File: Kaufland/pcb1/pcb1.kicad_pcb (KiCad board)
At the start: 2 copper layers, 118.4 x 66.5 mm, 15 parts, among them J1 AudioJack2, J2 Barrel_Jack, SW1 SW_Push, U1 DF_Player, U2 RGB_LED_STRIP

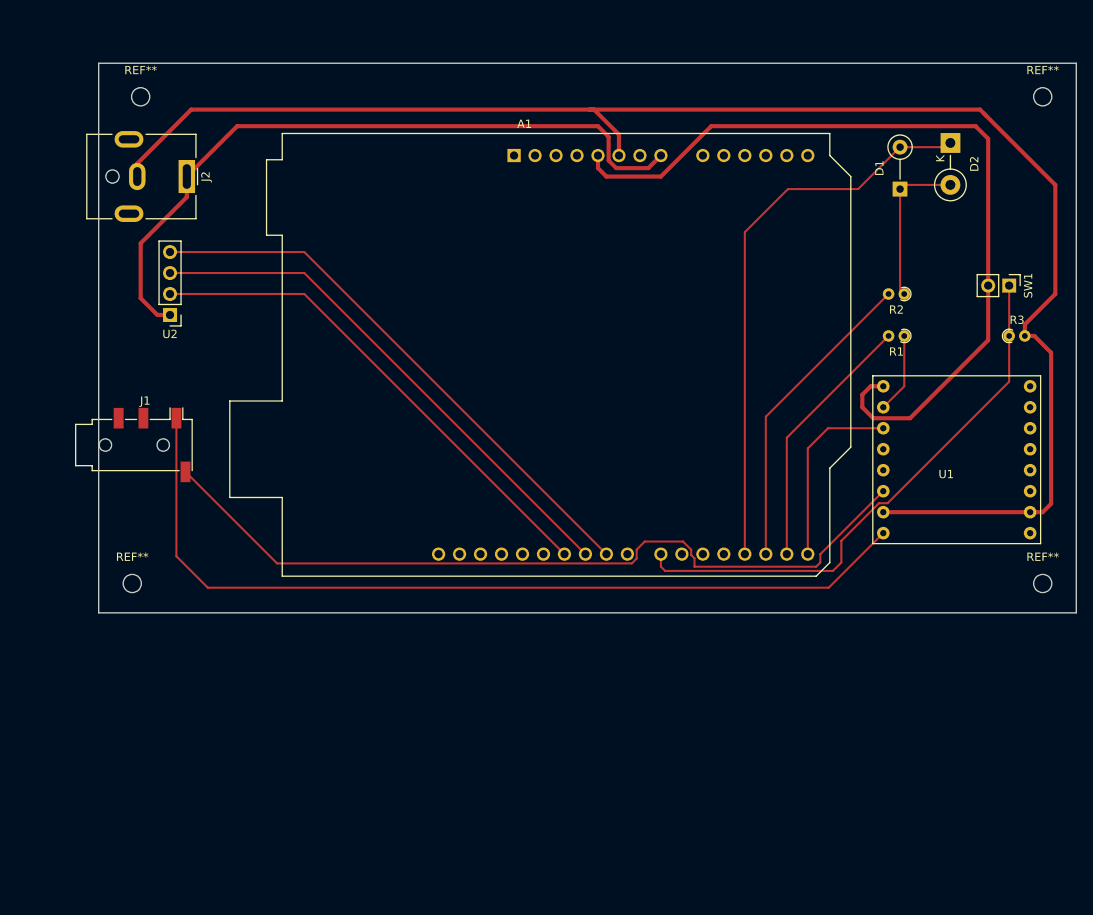
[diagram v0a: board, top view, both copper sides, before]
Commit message: Flipped pcb (to be checked; routed)
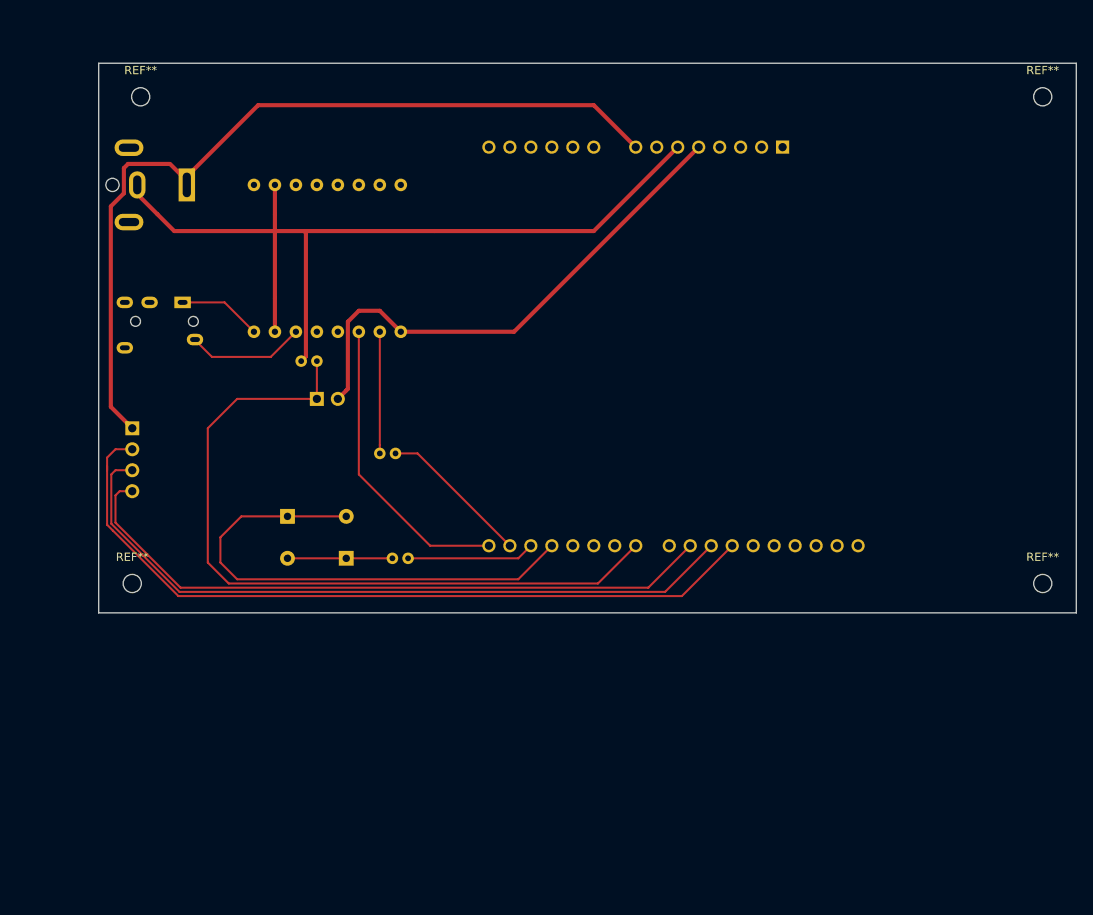
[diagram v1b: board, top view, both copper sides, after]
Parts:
- A1, D1, J2, R1, R2, R3, SW1, U1, U2: moved to B.Cu
- D2: footprint Diode_THT:D_DO-15_P5.08mm_Vertical_KathodeUp -> Diode_THT:D_A-405_P5.08mm_Vertical_KathodeUp; moved to B.Cu
- J1: footprint Connector_Audio:Jack_3.5mm_PJ320D_Horizontal -> Connector_Audio:Jack_3.5mm_PJ320E_Horizontal; moved to B.Cu
- moved D2 92.1 mm to (72.6, 105.2)
- moved SW1 84.9 mm to (76.2, 90.9)
- moved R3 83.9 mm to (76.2, 86.4), turned to 180 degrees
- moved D1 80.6 mm to (79.8, 110.2)
- moved U1 80.0 mm to (76.2, 75.2), turned to 90 degrees
- moved R2 69.8 mm to (85.3, 110.2), turned to 0 degrees
- moved R1 65.1 mm to (83.8, 97.5), turned to 0 degrees
- moved A1 32.5 mm to (132.6, 60.5), turned to 180 degrees
- moved J1 17.9 mm to (59.9, 79.2), turned to 270 degrees
- moved U2 14.5 mm to (53.8, 94.5)
- moved J2 1.02 mm to (60.5, 65.0), turned to 90 degrees
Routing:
- net Net-(J1-PadT): track 106.6 -> 10.1 mm
- net GNDREF: track 189.8 -> 105.4 mm
- net Net-(J1-PadS): track 97.4 -> 14.4 mm
- net +5V: track 104.6 -> 63.2 mm
- net Net-(A1-Pad26): track 60.8 -> 93.9 mm
- net Net-(A1-Pad22): track 66.6 -> 90.3 mm
- net Net-(A1-Pad25): track 64.4 -> 87.1 mm
- net Net-(A1-Pad17): track 37.7 -> 15.5 mm
- net +12V: track 85.8 -> 103.0 mm
- net Net-(A1-Pad15): track 22.9 -> 36.6 mm
- net Net-(A1-Pad16): track 31.5 -> 18.5 mm
- net Net-(A1-Pad24): track 68.0 -> 80.5 mm
- net Net-(D1-Pad1): track 19.2 -> 12.7 mm
- net Net-(A1-Pad18): track 68.3 -> 62.0 mm
- net Net-(R1-Pad1): track 9.69 -> 14.7 mm

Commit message: small changes to the pcb
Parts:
- R1, R2, R3: footprint Resistor_THT:R_Axial_DIN0204_L3.6mm_D1.6mm_P1.90mm_Vertical -> Resistor_THT:R_Axial_DIN0204_L3.6mm_D1.6mm_P7.62mm_Horizontal
- moved R3 14.8 mm to (68.6, 99.1), turned to 90 degrees
- moved R1 6.37 mm to (86.9, 91.9), turned to 270 degrees
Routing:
- net GNDREF: track 105.4 -> 118.4 mm
- net Net-(A1-Pad22): track 90.3 -> 79.2 mm
- net Net-(A1-Pad16): track 18.5 -> 28.0 mm
- net Net-(A1-Pad17): track 15.5 -> 9.78 mm
- net Net-(R1-Pad1): track 14.7 -> 10.4 mm

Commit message: finished pcb v1.0
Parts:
- removed A1: Arduino_UNO_R3, Module:Arduino_UNO_R3
- removed J1: AudioJack2, Connector_Audio:Jack_3.5mm_PJ320E_Horizontal
- removed J2: Barrel_Jack, Connector_BarrelJack:BarrelJack_CUI_PJ-063AH_Horizontal
- removed R1: 1k, Resistor_THT:R_Axial_DIN0204_L3.6mm_D1.6mm_P7.62mm_Horizontal
- removed R2: 330, Resistor_THT:R_Axial_DIN0204_L3.6mm_D1.6mm_P7.62mm_Horizontal
- removed the REF** at (164.1, 54.4)
- removed the REF** at (164.1, 113.3)
- removed the REF** at (53.8, 113.3)
- removed the REF** at (54.9, 54.4)
- removed U1: DF_Player, pcb1:DFPlayerMini
- removed U2: RGB_LED_STRIP, Connector_PinHeader_2.54mm:PinHeader_1x04_P2.54mm_Vertical
- added Arduino: Arduino_UNO_R3, Module:Arduino_UNO_R3, F.Cu at (112.8, 63.5)
- added Audio jack: AudioJack2, Connector_Audio:Jack_3.5mm_PJ320E_Horizontal, F.Cu at (55.9, 77.7)
- added Barrel Jack: Barrel_Jack, Connector_BarrelJack:BarrelJack_CUI_PJ-063AH_Horizontal, F.Cu at (57.9, 99.6)
- added D3: LED, Connector:FanPinHeader_1x03_P2.54mm_Vertical, F.Cu at (124.5, 121.9)
- added D4: LED, Connector:FanPinHeader_1x03_P2.54mm_Vertical, F.Cu at (127.0, 131.6)
- added DF Player: DF_Player, pcb1:DFPlayerMini, F.Cu at (66.5, 58.4)
- added Q1: IRLB8721PBF, Package_TO_SOT_THT:TO-220-3_Vertical, F.Cu at (50.8, 124.5)
- added Q2: IRLB8721PBF, Package_TO_SOT_THT:TO-220-3_Vertical, F.Cu at (53.3, 132.6)
- added Q3: IRLB8721PBF, Package_TO_SOT_THT:TO-220-3_Vertical, F.Cu at (55.9, 140.7)
- added Q4: IRLB8721PBF, Package_TO_SOT_THT:TO-220-3_Vertical, F.Cu at (91.9, 134.1)
- added Q5: IRLB8721PBF, Package_TO_SOT_THT:TO-220-3_Vertical, F.Cu at (100.1, 131.6)
- added Q6: IRLB8721PBF, Package_TO_SOT_THT:TO-220-3_Vertical, F.Cu at (108.2, 129.0)
- added R1 1k: 1k, Resistor_THT:R_Axial_DIN0204_L3.6mm_D1.6mm_P7.62mm_Horizontal, F.Cu at (67.6, 83.8)
- added R2 330: 330, Resistor_THT:R_Axial_DIN0204_L3.6mm_D1.6mm_P7.62mm_Horizontal, F.Cu at (144.8, 128.0)
- added R4 330: 330, Resistor_THT:R_Axial_DIN0204_L3.6mm_D1.6mm_P7.62mm_Horizontal, F.Cu at (130.6, 127.5)
- added R5: 4.7k, Resistor_THT:R_Axial_DIN0204_L3.6mm_D1.6mm_P7.62mm_Horizontal, F.Cu at (117.0, 49.8)
- added REF**: MountingHole_2.2mm_M2, MountingHole:MountingHole_2.2mm_M2, F.Cu at (50.8, 48.3)
- added REF**: MountingHole_2.2mm_M2, MountingHole:MountingHole_2.2mm_M2, F.Cu at (153.4, 48.3)
- added REF**: MountingHole_2.2mm_M2, MountingHole:MountingHole_2.2mm_M2, F.Cu at (153.4, 147.8)
- added REF**: MountingHole_2.2mm_M2, MountingHole:MountingHole_2.2mm_M2, F.Cu at (50.8, 147.8)
- added RGB LED Strip 1: RGB_LED_STRIP-My_Library, Connector:FanPinHeader_1x04_P2.54mm_Vertical, F.Cu at (53.3, 114.3)
- added RGB LED Strip 2: RGB_LED_STRIP-My_Library, Connector:FanPinHeader_1x04_P2.54mm_Vertical, F.Cu at (81.8, 131.6)
- added SW2: SW_Push, Connector:FanPinHeader_1x03_P2.54mm_Vertical, F.Cu at (122.9, 50.8)
- D1, D2: footprint Diode_THT:D_A-405_P5.08mm_Vertical_KathodeUp -> Connector:FanPinHeader_1x03_P2.54mm_Vertical; moved to F.Cu
- R3: moved to F.Cu
- SW1: footprint Connector_PinHeader_2.54mm:PinHeader_1x02_P2.54mm_Vertical -> Connector:FanPinHeader_1x03_P2.54mm_Vertical; moved to F.Cu
- moved D2 68.3 mm to (138.7, 122.4), turned to 0 degrees
- moved R3 66.9 mm to (113.9, 49.8), turned to 270 degrees
- moved D1 65.2 mm to (141.2, 132.0), turned to 180 degrees
- moved SW1 51.3 mm to (108.2, 50.8)
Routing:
- net GNDREF: track 118.4 -> 231.7 mm
- net Net-(A1-Pad18): track 0.00 -> 112.0 mm, vias 0 -> 3
- net Net-(A1-Pad20): track 0.00 -> 104.1 mm, vias 0 -> 3
- net Net-(A1-Pad21): track 0.00 -> 95.7 mm, vias 0 -> 3
- net Net-(A1-Pad28): track 0.00 -> 80.6 mm, vias 0 -> 2
- net Net-(A1-Pad15): track 36.6 -> 105.8 mm, vias 0 -> 1
- net Net-(A1-Pad25): track 87.1 -> 30.4 mm
- net Net-(A1-Pad24): track 80.5 -> 23.8 mm
- net Net-(A1-Pad26): track 93.9 -> 37.7 mm
- net Net-(A1-Pad16): track 28.0 -> 82.2 mm
- net Net-(A1-Pad19): track 62.0 -> 21.2 mm
- net +12V: track 103.0 -> 140.4 mm
- net Net-(Q3-Pad3): track 0.00 -> 26.4 mm
- net Net-(Q6-Pad3): track 0.00 -> 26.4 mm
- net Net-(A1-Pad22): track 0.00 -> 24.2 mm
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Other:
- board size 118.4 x 66.5 mm -> 109.7 x 106.7 mm
- board text added: "4,7k"
- board text added: "Audio sistem version: 1.0"

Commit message: Changed pins for LED strips
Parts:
- J1: renamed from Audio jack
- J2: renamed from Barrel Jack
- R1: renamed from R1 1k
- R2: renamed from R2 330
- R4: renamed from R4 330
- U1: renamed from DF Player
- U2: renamed from RGB LED Strip 1; footprint Connector:FanPinHeader_1x04_P2.54mm_Vertical -> Connector_JST:JST_EH_S4B-EH_1x04_P2.50mm_Horizontal
- U3: renamed from RGB LED Strip 2; footprint Connector:FanPinHeader_1x04_P2.54mm_Vertical -> Connector_JST:JST_EH_S4B-EH_1x04_P2.50mm_Horizontal
- moved U3 29.7 mm to (52.8, 138.2)
- moved Q2 26.2 mm to (79.2, 136.1)
- moved Q1 26.2 mm to (76.7, 128.0)
- moved Q3 26.2 mm to (81.8, 144.3)
- moved U2 7.13 mm to (52.8, 121.4), turned to 90 degrees
- moved Q4 0.51 mm to (91.9, 134.6)
- renumbered Arduino to A1
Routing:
- net Net-(Q3-Pad3): track 26.4 -> 68.1 mm
- net Net-(Q2-Pad3): track 18.3 -> 54.9 mm, vias 0 -> 1
- net Net-(Q5-Pad3): track 18.3 -> 51.3 mm, vias 0 -> 1
- net Net-(Q6-Pad3): track 26.4 -> 58.2 mm, vias 0 -> 1
- net Net-(Q4-Pad3): track 10.2 -> 41.7 mm
- net +12V: track 140.4 -> 112.1 mm
- net Net-(Q1-Pad3): track 10.2 -> 37.2 mm, vias 0 -> 4
- net GNDREF: track 231.7 -> 235.3 mm, vias 0 -> 1
- net Net-(A1-Pad21): track 95.7 -> 94.0 mm
- net Net-(A1-Pad20): track 104.1 -> 102.6 mm
- net Net-(A1-Pad18): track 112.0 -> 113.1 mm, vias 3 -> 2

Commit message: bugfixing pcb
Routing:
- net +12V: track 112.1 -> 131.1 mm
- net GNDREF: track 235.3 -> 234.2 mm, vias 1 -> 3
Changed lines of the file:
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@@
-(kicad_pcb (version 20171130) (host pcbnew "(5.1.6)-1")
+(kicad_pcb (version 20171130) (host pcbnew "(5.1.5)-3")
   (general
     (thickness 1.6)
     (drawings 12)
-    (tracks 236)
+    (tracks 246)
     (zones 0)
     (modules 27)
@@
   )
   (setup
-    (last_trace_width 0.25)
+    (last_trace_width 0.5)
     (user_trace_width 0.5)
     (trace_clearance 0.2)
@@
   (segment (start 108.712 120.396) (end 110.236 120.396) (width 0.25) (layer B.Cu) (net 11))
   (segment (start 118.876 111.76) (end 110.236 120.396) (width 0.25) (layer B.Cu) (net 11))
-  (segment (start 106.87899 123.422839) (end 107.873829 122.428) (width 0.25) (layer B.Cu) (net 13))
-  (segment (start 106.87899 124.81651) (end 106.87899 123.422839) (width 0.25) (layer B.Cu) (net 13))
+  (segment (start 110.744 122.428) (end 121.416 111.76) (width 0.25) (layer B.Cu) (net 13))
   (segment (start 100.076 131.572) (end 100.1235 131.572) (width 0.25) (layer B.Cu) (net 13))
+  (segment (start 106.87899 124.81651) (end 106.87899 123.24501) (width 0.25) (layer B.Cu) (net 13))
   (segment (start 100.1235 131.572) (end 106.87899 124.81651) (width 0.25) (layer B.Cu) (net 13))
-  (segment (start 110.748 122.428) (end 121.416 111.76) (width 0.25) (layer B.Cu) (net 13))
-  (segment (start 107.873829 122.428) (end 110.748 122.428) (width 0.25) (layer B.Cu) (net 13))
+  (segment (start 106.87899 123.24501) (end 107.696 122.428) (width 0.25) (layer B.Cu) (net 13))
+  (segment (start 107.696 122.428) (end 110.744 122.428) (width 0.25) (layer B.Cu) (net 13))
   (segment (start 123.956 111.76) (end 112.272 123.444) (width 0.25) (layer B.Cu) (net 15))
   (segment (start 112.272 123.444) (end 112.268 123.444) (width 0.25) (layer B.Cu) (net 15))
@@
   (segment (start 57.912 116.332) (end 52.832 121.412) (width 0.5) (layer B.Cu) (net 16))
   (segment (start 57.912 109.22) (end 57.912 116.332) (width 0.5) (layer B.Cu) (net 16))
+  (segment (start 51.857 121.412) (end 50.8 122.469) (width 0.5) (layer B.Cu) (net 16))
+  (segment (start 52.832 121.412) (end 51.857 121.412) (width 0.5) (layer B.Cu) (net 16))
+  (segment (start 50.8 122.469) (end 50.8 136.144) (width 0.5) (layer B.Cu) (net 16))
+  (segment (start 50.8 136.144) (end 52.832 138.176) (width 0.5) (layer B.Cu) (net 16))
   (segment (start 124.46 123.185) (end 124.46 131.572) (width 0.25) (layer F.Cu) (net 17))
   (segment (start 124.46 121.92) (end 124.46 123.185) (width 0.25) (layer F.Cu) (net 17))
@@
   (segment (start 131.581001 134.102999) (end 131.255999 134.428001) (width 0.25) (layer F.Cu) (net 19))
   (segment (start 130.556 111.76) (end 131.581001 112.785001) (width 0.25) (layer F.Cu) (net 19))
-  (segment (start 71.628 48.26) (end 71.628 66.04) (width 0.5) (layer B.Cu) (net 20))
   (segment (start 80.772 57.404) (end 82.804 57.404) (width 0.5) (layer B.Cu) (net 20))
   (segment (start 71.628 48.26) (end 80.772 57.404) (width 0.5) (layer B.Cu) (net 20))
-  (segment (start 113.88 57.448) (end 82.804 57.404) (width 0.5) (layer B.Cu) (net 20))
   (segment (start 82.804 57.404) (end 80.816 57.448) (width 0.5) (layer B.Cu) (net 20))
   (segment (start 113.88 57.448) (end 117.03 57.448) (width 0.5) (layer B.Cu) (net 20))
@@
   (segment (start 117.03 57.448) (end 119.424 57.448) (width 0.5) (layer B.Cu) (net 20))
   (segment (start 119.424 57.448) (end 124.676001 62.700001) (width 0.5) (layer B.Cu) (net 20))
-  (segment (start 75.380001 73.949999) (end 51.912 97.418) (width 0.5) (layer F.Cu) (net 20))
-  (segment (start 75.380001 65.458239) (end 75.380001 73.949999) (width 0.5) (layer F.Cu) (net 20))
   (segment (start 51.912 97.418) (end 51.912 99.568) (width 0.5) (layer F.Cu) (net 20))
-  (segment (start 74.749761 64.827999) (end 75.380001 65.458239) (width 0.5) (layer F.Cu) (net 20))
-  (segment (start 72.840001 64.827999) (end 74.749761 64.827999) (width 0.5) (layer F.Cu) (net 20))
-  (segment (start 71.628 66.04) (end 72.840001 64.827999) (width 0.5) (layer F.Cu) (net 20))
   (segment (start 48.71199 103.41801) (end 48.71199 108.14799) (width 0.5) (layer F.Cu) (net 20))
   (segment (start 51.912 99.568) (end 51.912 100.218) (width 0.5) (layer F.Cu) (net 20))
@@
   (segment (start 84.328 144.272) (end 84.328 144.3195) (width 0.5) (layer F.Cu) (net 20))
   (segment (start 50.292 109.728) (end 67.564 109.728) (width 0.5) (layer F.Cu) (net 20))
-  (segment (start 67.564 109.728) (end 68.58 110.744) (width 0.5) (layer F.Cu) (net 20))
-  (segment (start 68.58 110.744) (end 68.58 110.744) (width 0.25) (layer F.Cu) (net 20))
-  (via (at 68.58 110.744) (size 0.8) (drill 0.4) (layers F.Cu B.Cu) (net 20))
-  (segment (start 68.58 110.744) (end 78.232 110.744) (width 0.5) (layer B.Cu) (net 20))
+  (via (at 68.58 109.728) (size 0.8) (drill 0.4) (layers F.Cu B.Cu) (net 20))
   (segment (start 79.248 111.76) (end 79.248 128.016) (width 0.5) (layer B.Cu) (net 20))
   (segment (start 78.232 110.744) (end 79.248 111.76) (width 0.5) (layer B.Cu) (net 20))
@@
   (segment (start 94.996 129.032) (end 91.948 132.08) (width 0.5) (layer F.Cu) (net 20))
   (segment (start 100.076 129.032) (end 94.996 129.032) (width 0.5) (layer F.Cu) (net 20))
+  (segment (start 67.564 109.728) (end 68.58 109.728) (width 0.5) (layer F.Cu) (net 20))
+  (segment (start 79.248 111.76) (end 77.216 109.728) (width 0.5) (layer B.Cu) (net 20))
+  (segment (start 77.216 109.728) (end 68.58 109.728) (width 0.5) (layer B.Cu) (net 20))
+  (segment (start 51.912 97.418) (end 51.912 99.568) (width 0.5) (layer B.Cu) (net 20))
+  (segment (start 62.97 86.36) (end 62.97 86.36) (width 0.5) (layer B.Cu) (net 20))
+  (segment (start 62.97 86.36) (end 51.912 97.418) (width 0.5) (layer B.Cu) (net 20))
+  (via (at 62.97 86.36) (size 0.8) (drill 0.4) (layers F.Cu B.Cu) (net 20))
+  (segment (start 62.97 86.36) (end 62.97 81.302) (width 0.5) (layer F.Cu) (net 20))
+  (segment (start 62.97 81.302) (end 74.676 69.596) (width 0.5) (layer F.Cu) (net 20))
+  (segment (start 74.676 69.596) (end 74.676 69.596) (width 0.5) (layer F.Cu) (net 20))
+  (via (at 74.676 69.596) (size 0.8) (drill 0.4) (layers F.Cu B.Cu) (net 20))
+  (segment (start 71.628 66.04) (end 71.628 66.04) (width 0.5) (layer B.Cu) (net 20))
+  (segment (start 71.628 66.548) (end 74.676 69.596) (width 0.5) (layer B.Cu) (net 20))
+  (segment (start 71.628 66.04) (end 71.628 66.548) (width 0.5) (layer B.Cu) (net 20))
+  (segment (start 74.676 69.596) (end 86.868 57.404) (width 0.5) (layer B.Cu) (net 20))
+  (segment (start 113.88 57.448) (end 86.868 57.404) (width 0.5) (layer B.Cu) (net 20))
+  (segment (start 86.868 57.404) (end 82.804 57.404) (width 0.5) (layer B.Cu) (net 20))
   (segment (start 66.04 115.316) (end 66.04 122.936) (width 0.25) (layer F.Cu) (net 21))
   (segment (start 133.096 111.76) (end 129.54 108.204) (width 0.25) (layer F.Cu) (net 21))
@@
   (segment (start 67.564 128.016) (end 76.708 128.016) (width 0.25) (layer B.Cu) (net 21))
   (segment (start 108.204 53.34) (end 122.936 53.34) (width 0.5) (layer F.Cu) (net 22))
-  (segment (start 123.735999 62.700001) (end 122.936 63.5) (width 0.5) (layer F.Cu) (net 22))
-  (segment (start 124.46 61.976) (end 123.735999 62.700001) (width 0.5) (layer F.Cu) (net 22))
-  (segment (start 124.46 53.349) (end 124.46 61.976) (width 0.5) (layer F.Cu) (net 22))
-  (segment (start 124.451 53.34) (end 124.46 53.349) (width 0.5) (layer F.Cu) (net 22))
-  (segment (start 122.936 53.34) (end 124.451 53.34) (width 0.5) (layer F.Cu) (net 22))
   (segment (start 69.088 53.34) (end 108.204 53.34) (width 0.5) (layer F.Cu) (net 22))
   (segment (start 56.388 66.04) (end 69.088 53.34) (width 0.5) (layer F.Cu) (net 22))
+  (segment (start 123.735999 62.700001) (end 122.936 63.5) (width 0.5) (layer F.Cu) (net 22))
+  (segment (start 124.968 61.468) (end 123.735999 62.700001) (width 0.5) (layer F.Cu) (net 22))
+  (segment (start 122.936 53.34) (end 124.968 55.372) (width 0.5) (layer F.Cu) (net 22))
+  (segment (start 124.968 55.372) (end 124.968 61.468) (width 0.5) (layer F.Cu) (net 22))
   (segment (start 79.248 136.144) (end 79.933829 136.144) (width 0.25) (layer B.Cu) (net 23))
   (segment (start 135.636 111.76) (end 130.556 106.68) (width 0.25) (layer F.Cu) (net 23))
